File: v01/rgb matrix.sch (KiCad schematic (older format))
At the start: 76 parts, among them U3 IS31FL3733-TQ, U4 IS31FL3733-TQ

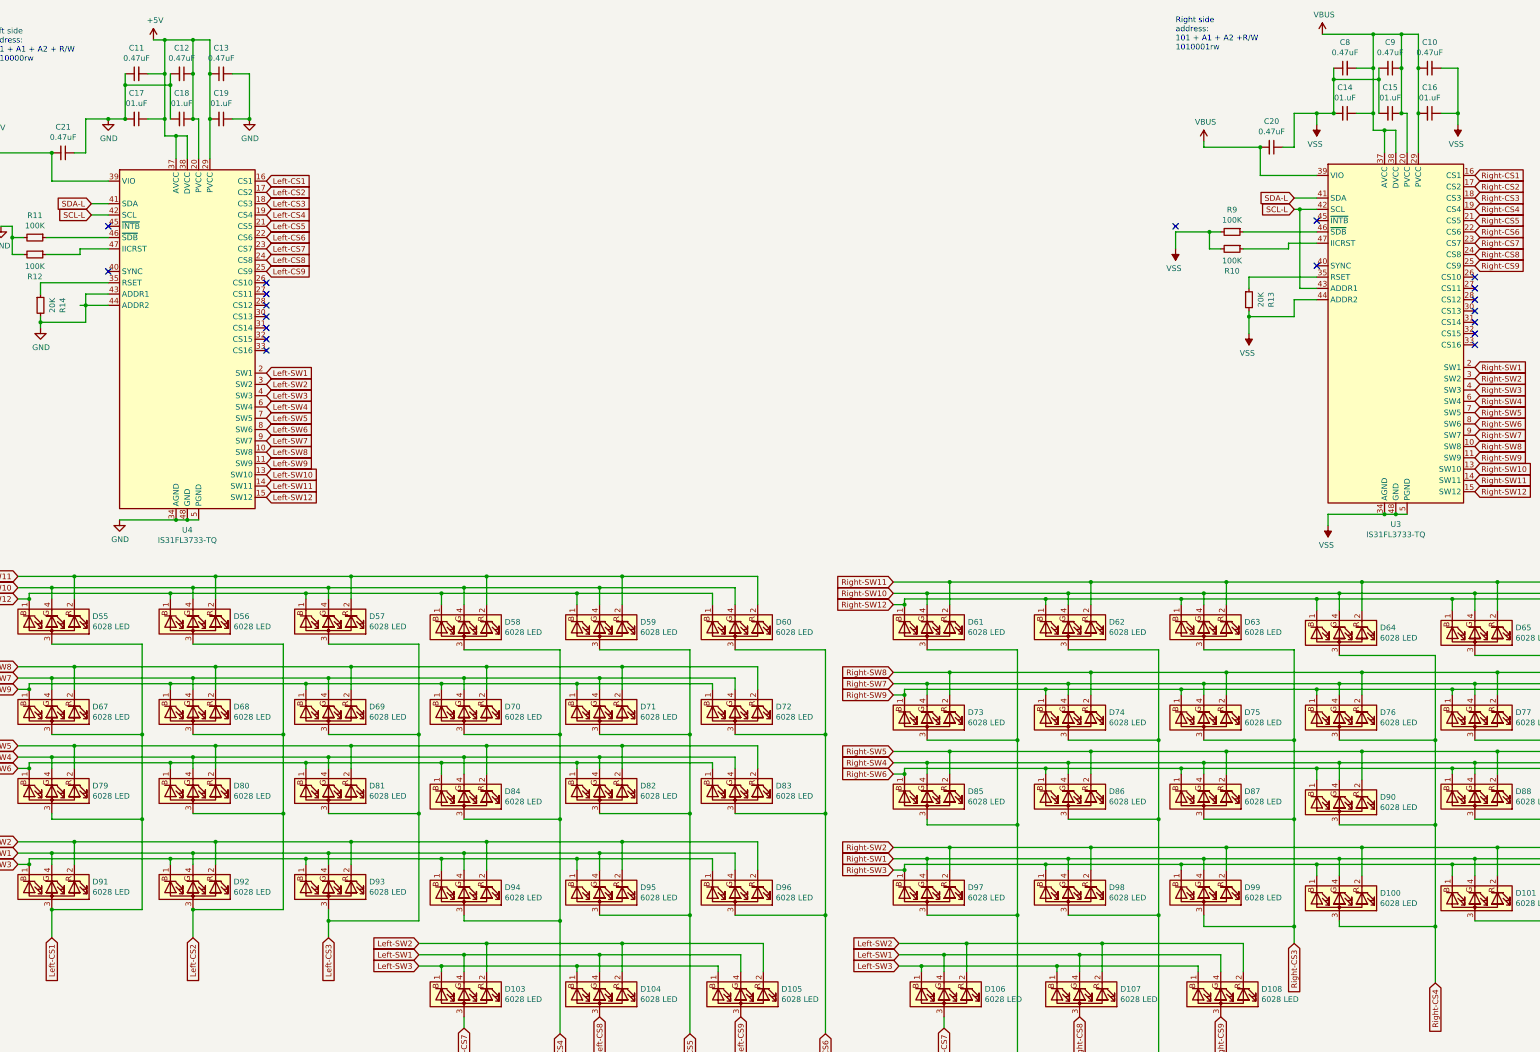
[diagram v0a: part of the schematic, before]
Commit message: More routing progress on RGB matrix
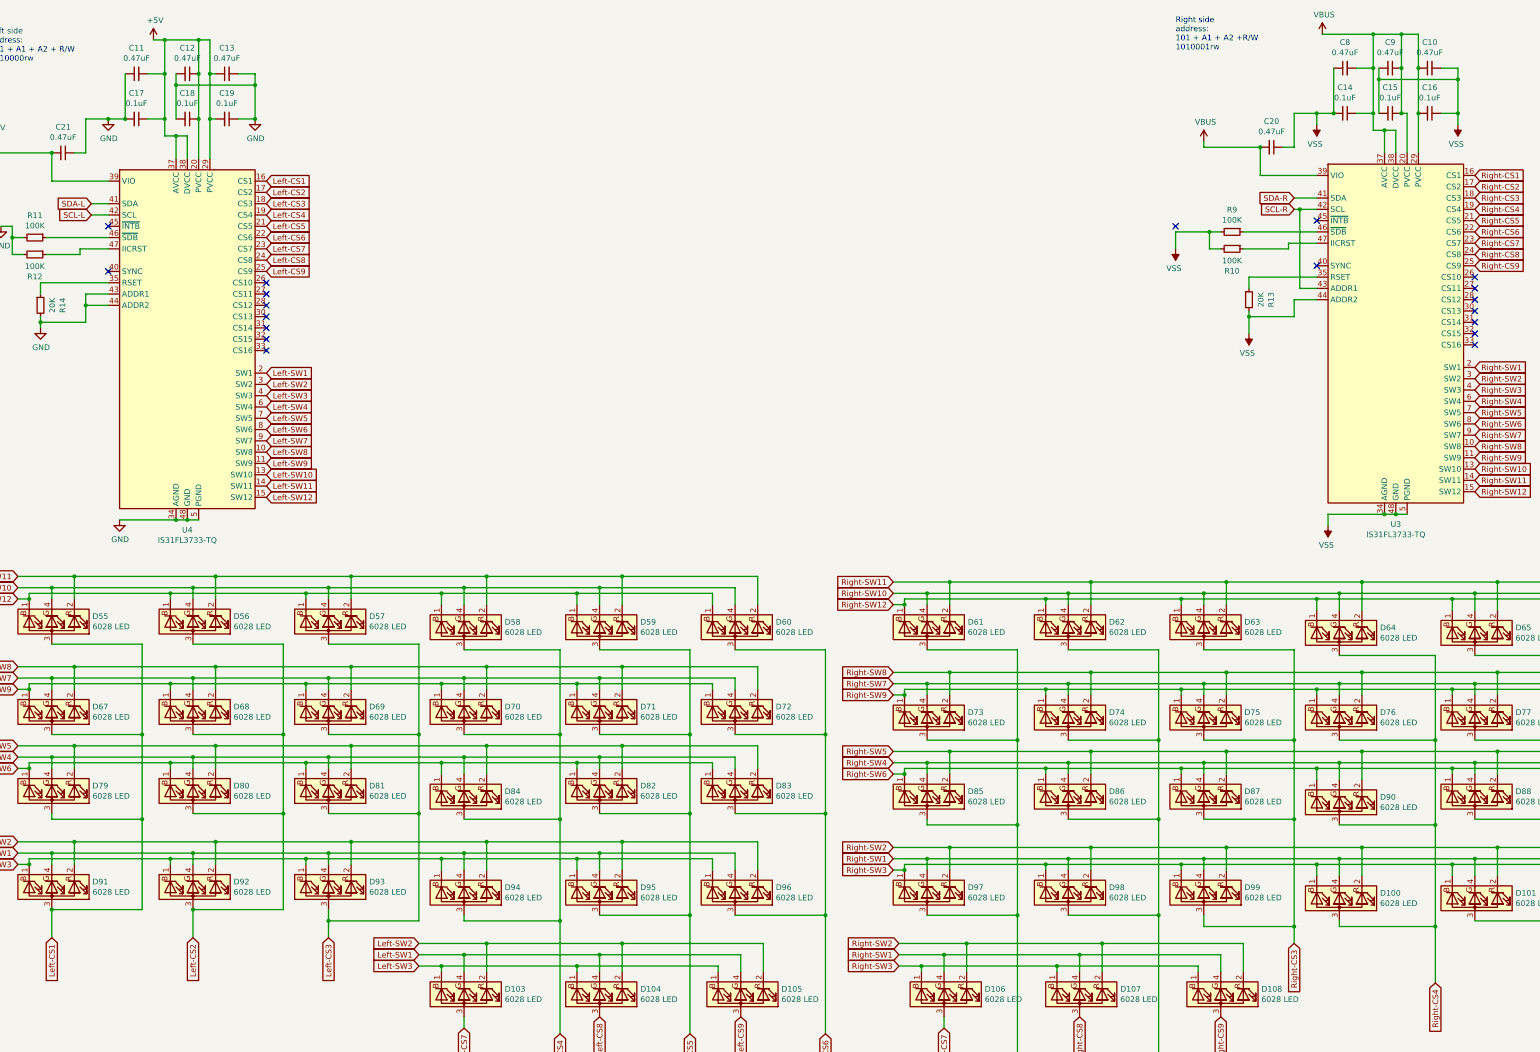
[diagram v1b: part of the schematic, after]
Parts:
- C10, C11, C12, C13, C20, C21, C8, C9: footprint (none) -> Capacitor_SMD:C_0805_2012Metric
- C14, C15, C16, C17, C18, C19: value 01.uF -> 0.1uF; footprint (none) -> Capacitor_SMD:C_0805_2012Metric
- D100, D101, D102, D103, D104, D105, D106, D107, D108, D55, D56, D57, D58, D59, D60, D61, D62, D63, D64, D65, D66, D67, D68, D69, D70, D71, D72, D73, D74, D75, D76, D77, D78, D79, D80, D81, D82, D83, D84, D85, D86, D87, D88, D89, D90, D91, D92, D93, D94, D95, D96, D97, D98, D99: footprint (none) -> Keebio-Parts:RGB_3528_Blue_Notch-MX
- R10, R11, R12, R13, R14, R9: footprint (none) -> Resistor_SMD:R_0805_2012Metric
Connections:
- net Left-SW1: no longer D106.4 (GK), D107.4 (GK), D108.4 (GK)
- net Left-SW2: no longer D106.2 (RK), D107.2 (RK), D108.2 (RK)
- net Left-SW3: no longer D106.1 (BK), D107.1 (BK), D108.1 (BK)
- net Right-SW1: now also D106.4 (GK), D107.4 (GK), D108.4 (GK)
- net Right-SW2: now also D106.2 (RK), D107.2 (RK), D108.2 (RK)
- net Right-SW3: now also D106.1 (BK), D107.1 (BK), D108.1 (BK)
- net SCL-L: no longer U3.42 (SCL), U3.43 (ADDR1)
- net SDA-L: no longer U3.41 (SDA)
- new net SCL-R: U3.42 (SCL), U3.43 (ADDR1)
- new net SDA-R: U3.41 (SDA)
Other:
- moved on the sheet: C12, C13, C18, C19
